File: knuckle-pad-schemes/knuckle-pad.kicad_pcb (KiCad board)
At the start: 2 copper layers, 128.7 x 116.2 mm, 66 parts, among them SW1 SW_Push, SW10 SW_Push, SW11 SW_Push, SW12 SW_Push, SW13 SW_Push, SW14 SW_Push, SW15 SW_Push, SW16 SW_Push, SW17 SW_Push, SW18 SW_Push, SW19 SW_Push, SW2 SW_Push, SW20 SW_Push, SW21 SW_Push, SW22 SW_Push, SW23 SW_Push, SW24 SW_Push, SW25 SW_Push, SW26 SW_Push, SW27 SW_Push, SW28 SW_Push, SW29 SW_Push, SW3 SW_Push, SW30 SW_Push, SW4 SW_Push, SW5 SW_Push, SW6 SW_Push, SW7 SW_Push, SW8 SW_Push, SW9 SW_Push, U1 ProMicro

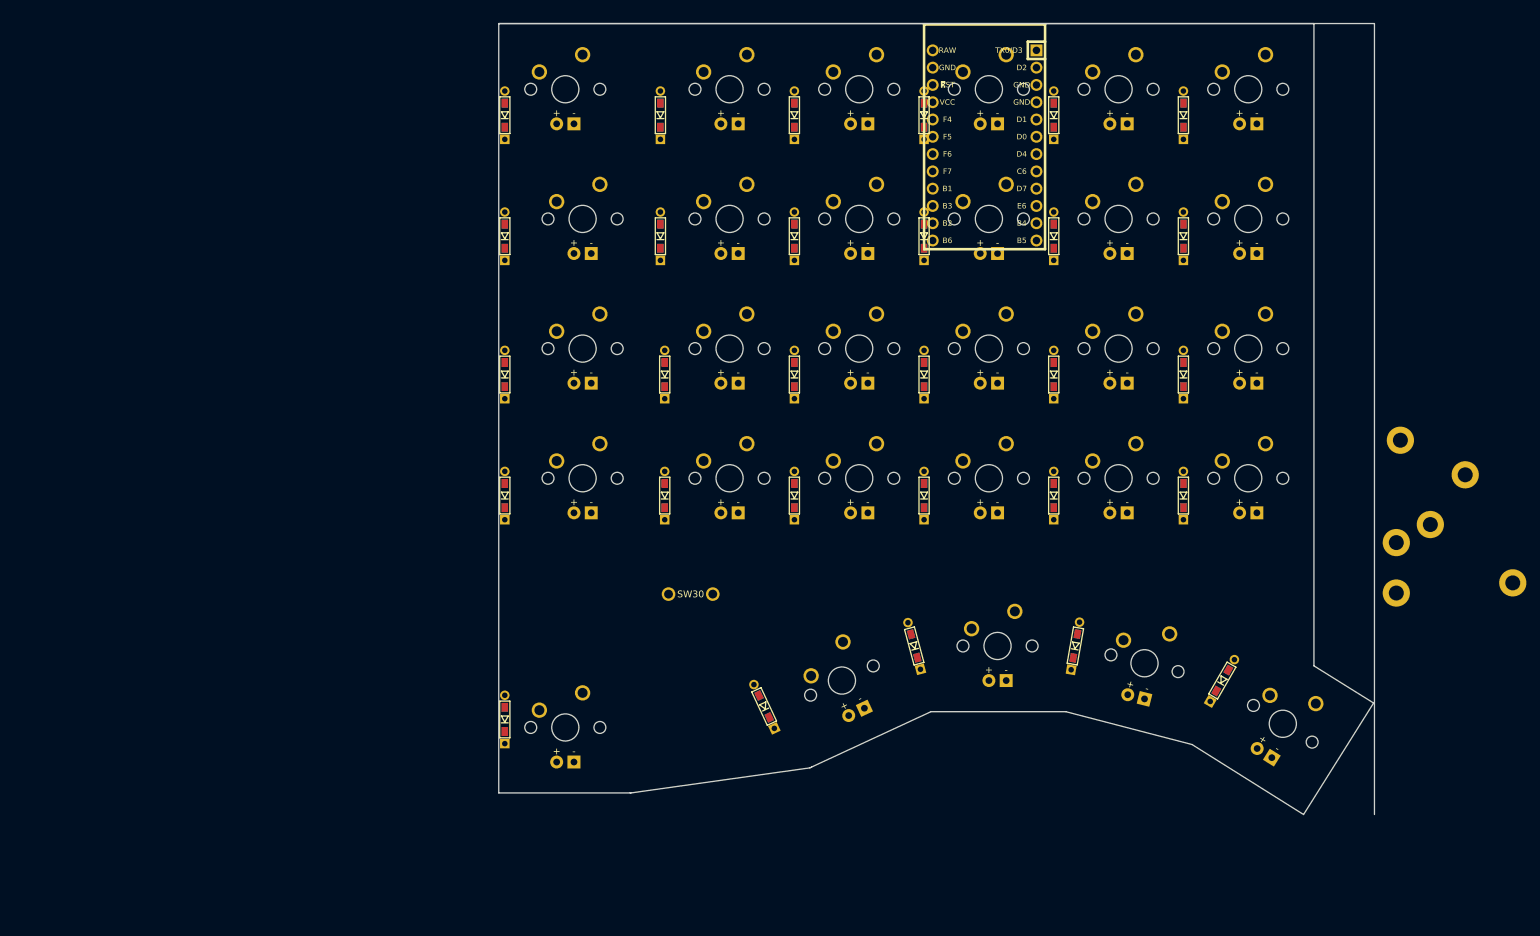
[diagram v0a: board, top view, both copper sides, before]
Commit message: updated pcb shape to (preliminary) final+added pwr_flag to schematic
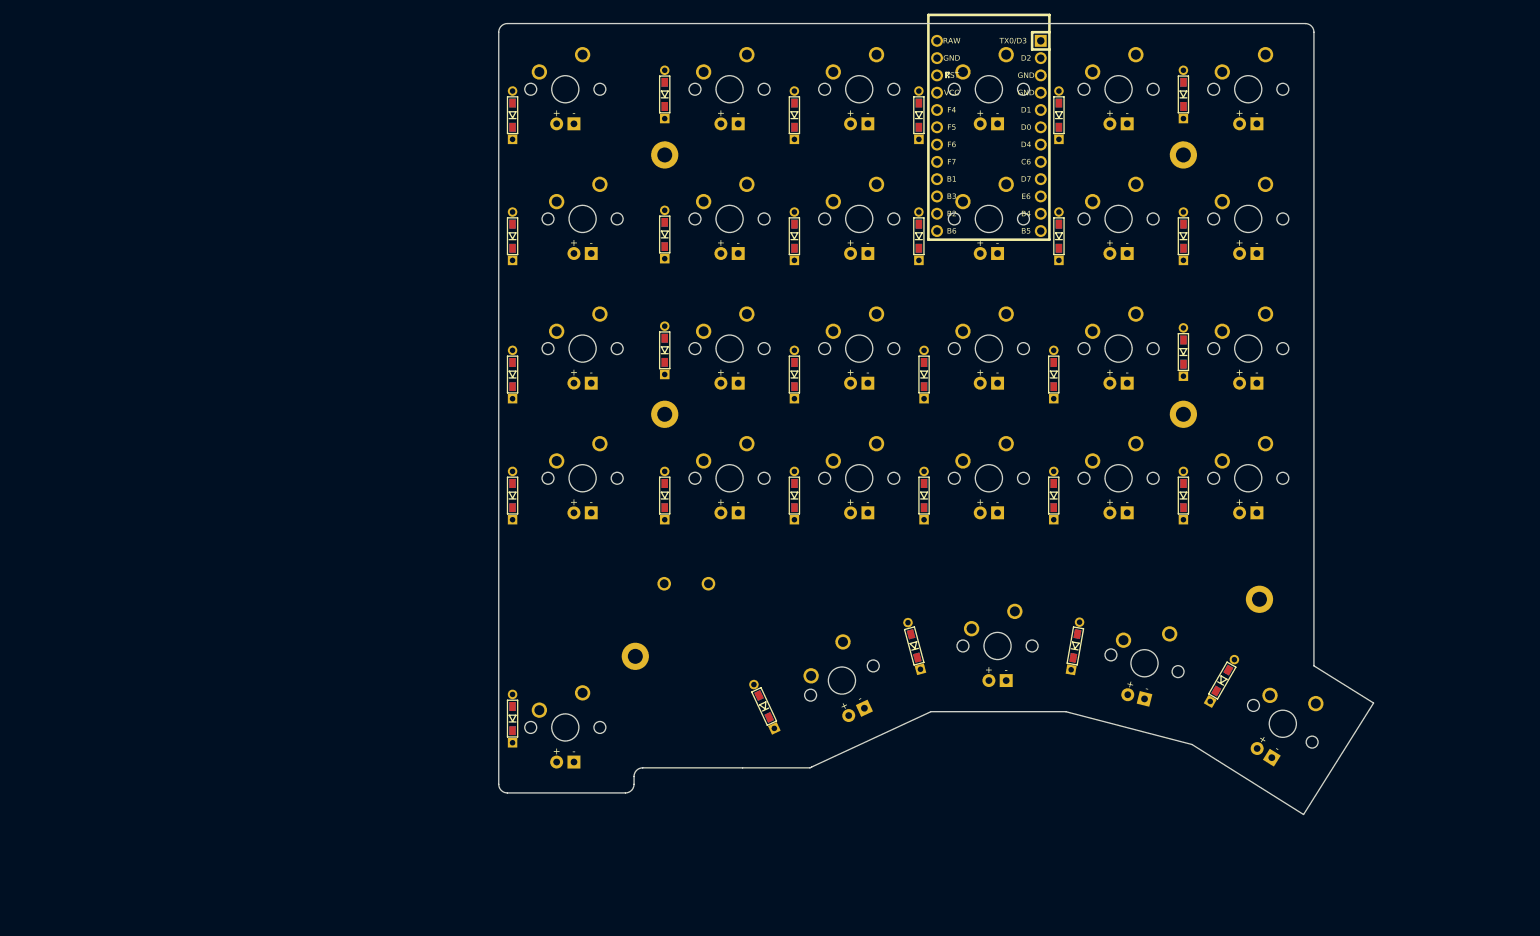
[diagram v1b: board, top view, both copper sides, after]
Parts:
- RST1: renamed from SW30; moved to B.Cu
- moved H3 129.4 mm to (172.2, 110.0)
- moved H2 121.6 mm to (176.5, 36.3)
- moved H4 110.6 mm to (176.5, 74.4)
- moved H5 52.7 mm to (252.7, 36.3)
- moved H1 39.7 mm to (252.7, 74.4)
- moved H6 35.3 mm to (263.9, 101.6)
- moved D8 3.56 mm to (176.5, 65.0)
- moved D27 3.30 mm to (252.7, 65.3)
- moved D6 3.11 mm to (176.5, 27.4)
- moved D25 3.05 mm to (252.7, 27.4)
- moved RST1 1.65 mm to (179.7, 99.3), turned to 180 degrees
- moved U1 1.53 mm to (224.2, 33.5)
- moved D5 1.15 mm to (154.2, 119.1)
- moved D1 1.14 mm to (154.2, 30.5)
- moved D2 1.14 mm to (154.2, 48.3)
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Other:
- board size 128.7 x 116.2 mm -> 128.5 x 116.2 mm

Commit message: push before routing
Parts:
- moved RST1 99.3 mm to (238.4, 19.3)
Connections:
- U1 pad 2: row0 -> Net-(U1-Pad2)
- U1 pad 5: row1 -> Net-(U1-Pad5)
- U1 pad 6: Net-(U1-Pad6) -> row0
- U1 pad 9: Net-(U1-Pad9) -> row1

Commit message: rounded all edges(
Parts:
- D1, D10, D11, D12, D13, D14, D15, D16, D17, D18, D19, D2, D20, D21, D22, D23, D24, D25, D26, D27, D28, D29, D3, D4, D5, D6, D7, D8, D9, RST1, U1: moved to F.Cu
- H1, H2, H3, H4, H5, H6, SW1, SW10, SW11, SW12, SW13, SW14, SW15, SW16, SW17, SW18, SW19, SW2, SW20, SW21, SW22, SW23, SW24, SW25, SW26, SW27, SW28, SW29, SW3, SW4, SW5, SW6, SW7, SW8, SW9: moved to B.Cu
- moved SW29 162.0 mm to (105.4, 126.0), turned to 212 degrees
- moved H6 155.2 mm to (108.8, 107.7), turned to 180 degrees
- moved SW25 151.9 mm to (110.5, 32.8), turned to 180 degrees
- moved SW26 151.9 mm to (110.5, 51.8), turned to 180 degrees
- moved SW27 151.9 mm to (110.5, 70.9), turned to 180 degrees
- moved SW28 151.9 mm to (110.5, 89.9), turned to 180 degrees
- moved D29 144.3 mm to (114.3, 119.6), turned to 120 degrees
- moved D27 132.9 mm to (120.0, 72.1)
- moved D26 132.9 mm to (119.9, 52.9)
- moved D25 132.9 mm to (120.0, 33.5)
- moved H1 132.9 mm to (120.0, 80.5), turned to 180 degrees
- moved H5 132.9 mm to (120.0, 42.4), turned to 180 degrees
- moved D28 132.7 mm to (120.1, 91.1)
- moved SW24 121.4 mm to (125.7, 117.1), turned to 194 degrees
- moved SW20 113.8 mm to (129.5, 32.8), turned to 180 degrees
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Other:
- board size 128.5 x 116.2 mm -> 127.6 x 115.3 mm

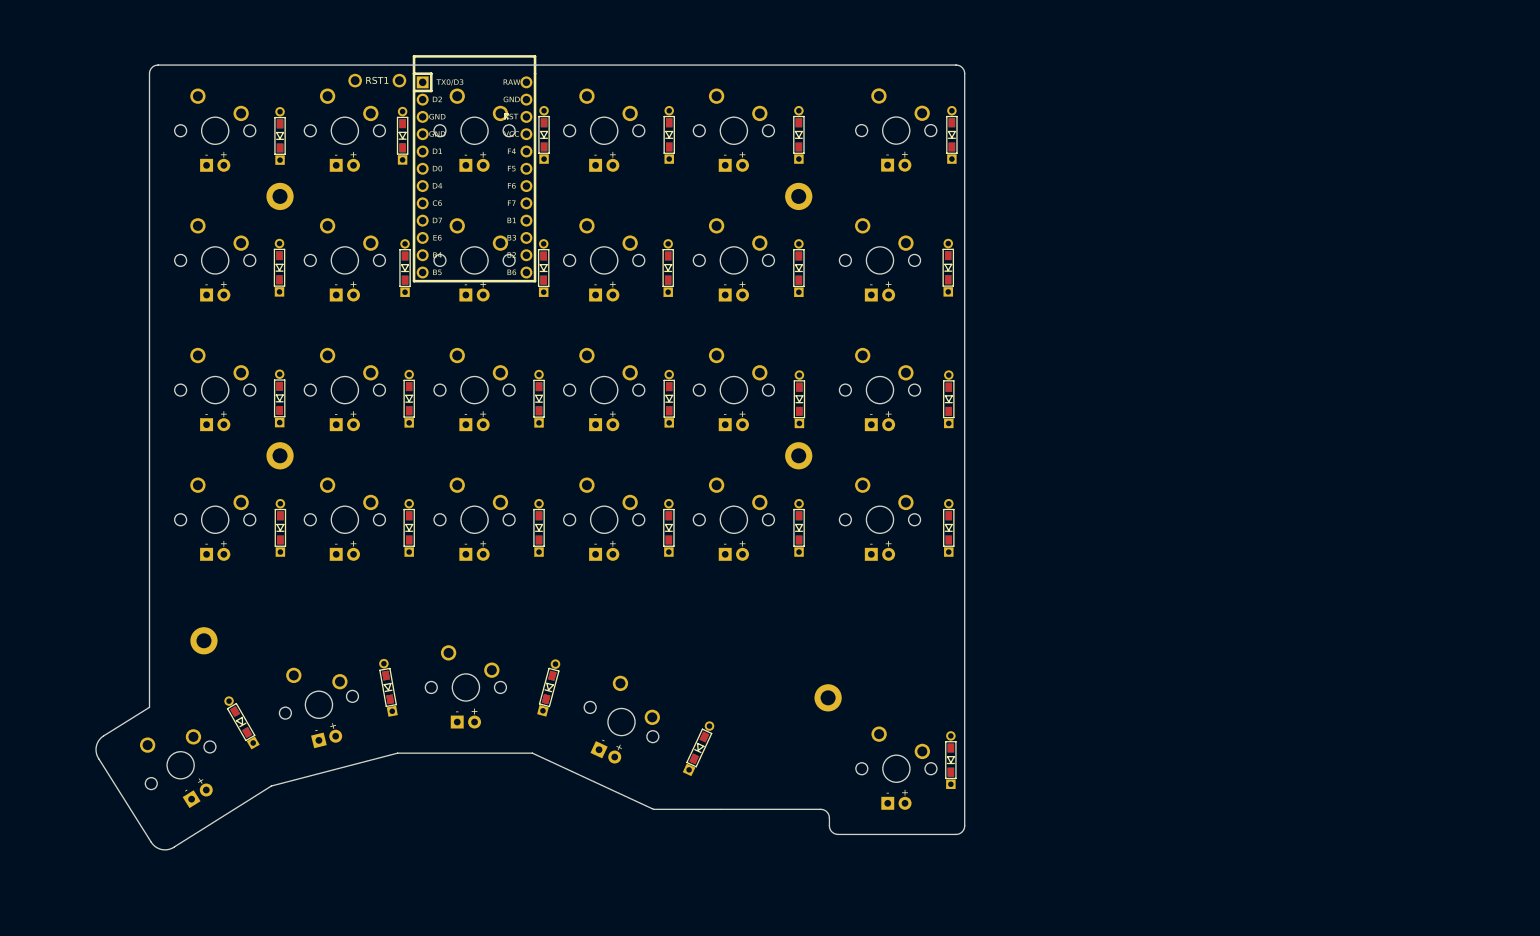
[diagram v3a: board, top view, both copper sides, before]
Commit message: added 1st routing, needs optimization
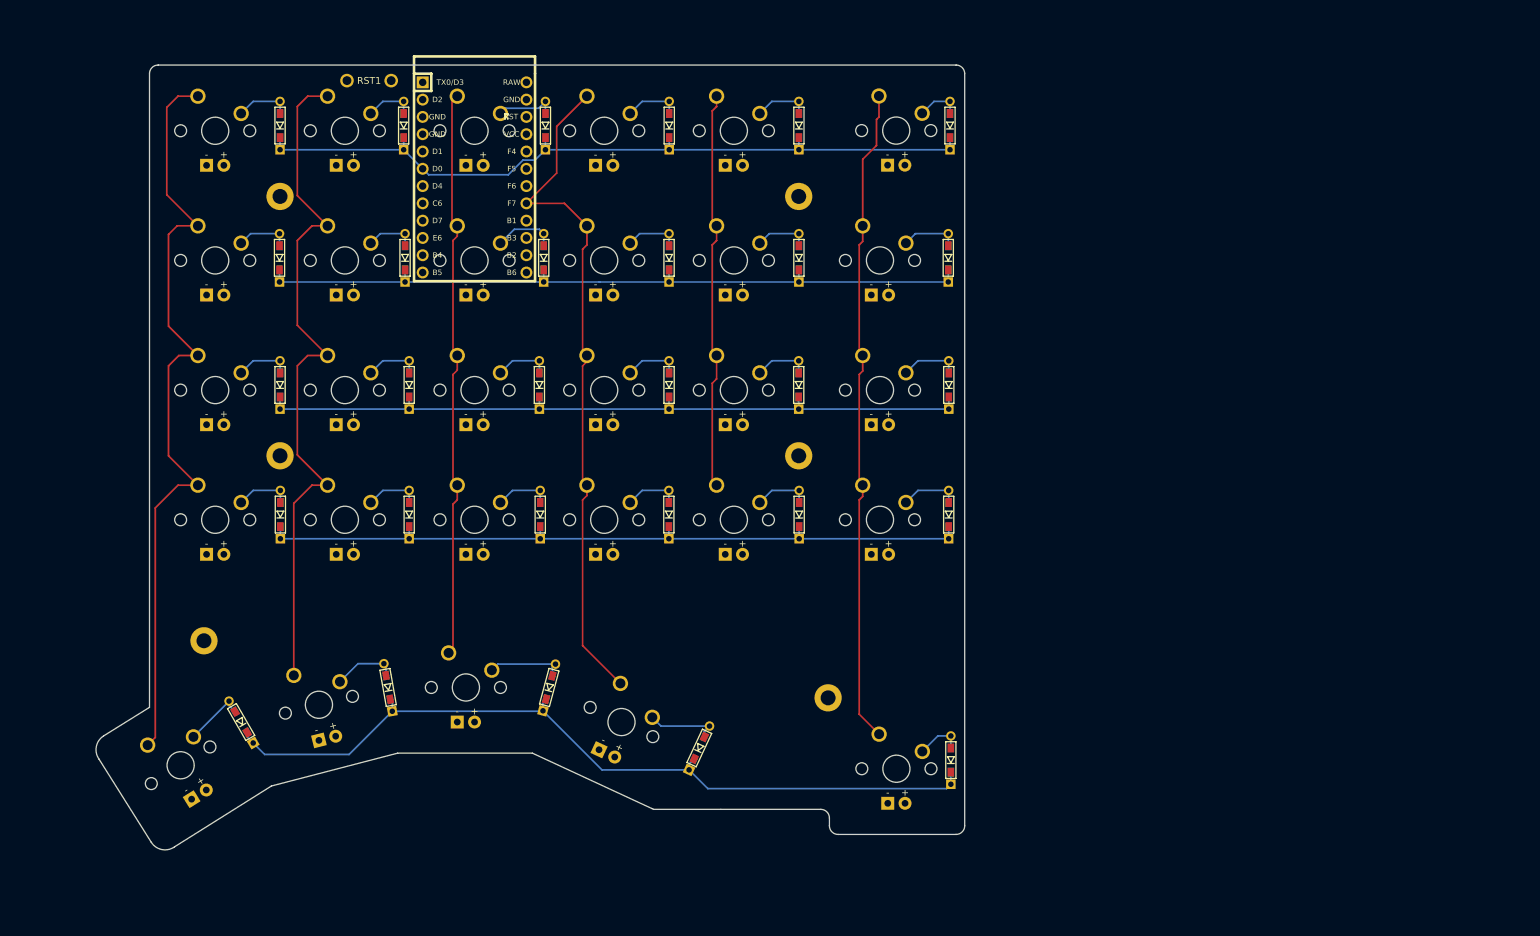
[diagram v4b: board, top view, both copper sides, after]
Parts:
- moved D8 2.10 mm to (196.2, 70.1)
- moved D3 2.10 mm to (218.3, 70.1)
- moved D17 2.03 mm to (158.1, 70.1)
- moved D12 2.03 mm to (177.2, 70.1)
- moved D22 2.02 mm to (139.0, 70.1)
- moved D27 1.98 mm to (120.0, 70.1)
- moved D18 1.96 mm to (158.2, 89.2)
- moved D13 1.96 mm to (177.1, 89.2)
- moved D28 1.96 mm to (120.1, 89.2)
- moved D4 1.95 mm to (218.2, 89.2)
- moved D23 1.95 mm to (139.0, 89.2)
- moved D9 1.95 mm to (196.3, 89.2)
- moved D25 1.52 mm to (120.0, 32.0)
- moved D21 1.50 mm to (138.4, 51.4)
- moved D7 1.50 mm to (196.2, 51.4)
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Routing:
- net row4: track 0.00 -> 120.2 mm
- net col5: track 0.00 -> 116.2 mm
- net row0: track 0.00 -> 112.1 mm
- net row1: track 0.00 -> 108.9 mm
- net row2: track 0.00 -> 108.9 mm
- net row3: track 0.00 -> 108.8 mm
- net col4: track 0.00 -> 104.3 mm
- net col2: track 0.00 -> 100.5 mm
- net col0: track 0.00 -> 97.0 mm
- net col3: track 0.00 -> 84.0 mm
- net col1: track 0.00 -> 58.7 mm
- net Net-(D19-Pad2): track 0.00 -> 11.6 mm
- net Net-(D14-Pad2): track 0.00 -> 10.9 mm
- net Net-(D24-Pad2): track 0.00 -> 9.43 mm
- net Net-(D29-Pad2): track 0.00 -> 9.32 mm
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
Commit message: finished routing
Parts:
- moved RST1 39.1 mm to (172.2, 25.4)
- moved D1 19.1 mm to (199.4, 32.0)
- moved D3 18.8 mm to (199.4, 70.1)
- moved D2 18.8 mm to (199.4, 51.1)
- moved D4 18.8 mm to (199.5, 89.2)
- moved D5 18.1 mm to (200.5, 125.5)
- moved H3 8.41 mm to (201.2, 107.7)
- moved H6 3.94 mm to (112.8, 107.7)
- moved D16 0.83 mm to (159.5, 51.1)
- moved D21 0.65 mm to (137.9, 51.1)
- moved D15 0.46 mm to (159.5, 32.0)
- moved D26 0.39 mm to (120.0, 51.1)
- moved D7 0.38 mm to (196.3, 51.1)
- moved D20 0.38 mm to (137.8, 32.0)
- moved D11 0.38 mm to (177.2, 51.1)
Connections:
- U1 pad 14: col5 -> Net-(U1-Pad14)
- U1 pad 15: col4 -> Net-(U1-Pad15)
- U1 pad 5: Net-(U1-Pad5) -> row0
- U1 pad 6: row0 -> col5
- U1 pad 7: Net-(U1-Pad7) -> col4
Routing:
- net row4: track 120.2 -> 177.3 mm
- net col0: track 97.0 -> 151.4 mm
- net row3: track 108.8 -> 144.7 mm
- net GND: track 0.00 -> 32.7 mm
- net col1: track 58.7 -> 90.3 mm
- net RST: track 0.00 -> 21.8 mm
- net col5: track 116.2 -> 136.8 mm
- net row2: track 108.9 -> 128.1 mm
- net Net-(D1-Pad2): track 6.59 -> 19.2 mm
- net col3: track 84.0 -> 95.6 mm
- net Net-(D5-Pad2): track 6.91 -> 18.3 mm
- net row0: track 112.1 -> 101.7 mm
- net Net-(D2-Pad2): track 8.57 -> 16.9 mm
- net Net-(D3-Pad2): track 8.81 -> 16.8 mm
- net Net-(D4-Pad2): track 8.79 -> 16.8 mm
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
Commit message: added logo and finalized routing
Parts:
- added G***: LOGO, Hybrid-Switches:logo_fin, F.Cu at (94.7, 118.1)
- D1, D10, D11, D12, D13, D14, D15, D16, D17, D18, D19, D2, D20, D21, D22, D23, D24, D25, D26, D27, D28, D29, D3, D4, D5, D6, D7, D8, D9, RST1, U1: moved to B.Cu
- H1, H2, H3, H4, H5, H6, SW1, SW10, SW11, SW12, SW13, SW14, SW15, SW16, SW17, SW18, SW19, SW2, SW20, SW21, SW22, SW23, SW24, SW25, SW26, SW27, SW28, SW29, SW3, SW4, SW5, SW6, SW7, SW8, SW9: moved to F.Cu
- moved SW5 120.1 mm to (90.9, 137.2), turned to 0 degrees
- moved SW1 120.1 mm to (91.0, 43.4), turned to 0 degrees
- moved SW2 115.3 mm to (93.3, 62.5), turned to 0 degrees
- moved SW3 115.3 mm to (93.3, 81.5), turned to 0 degrees
- moved SW4 115.3 mm to (93.3, 100.6), turned to 0 degrees
- moved D5 100.0 mm to (101.0, 136.2)
- moved D4 98.0 mm to (102.0, 99.8)
- moved D3 97.9 mm to (102.1, 80.8)
- moved D1 97.9 mm to (102.1, 42.7)
- moved D2 97.9 mm to (102.1, 61.7)
- moved H3 91.9 mm to (110.7, 124.2), turned to 0 degrees
- moved D7 91.7 mm to (105.2, 61.7)
- moved D9 91.7 mm to (105.2, 99.8)
- moved D6 91.6 mm to (105.3, 42.7)
- moved D8 91.6 mm to (105.3, 80.8)
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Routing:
- net col5: track 136.8 -> 140.9 mm
- net row2: track 128.1 -> 129.0 mm
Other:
- outline, holes or cut-outs redrawn
- board text added: "knuckle-pad"
